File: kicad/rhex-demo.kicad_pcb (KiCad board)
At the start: 2 copper layers, 58 parts, among them J1 MCU power, M1 Motor_Servo, M2 Motor_Servo, M3 Motor_Servo, M4 Motor_Servo, M5 Motor_Servo, M6 Motor_Servo

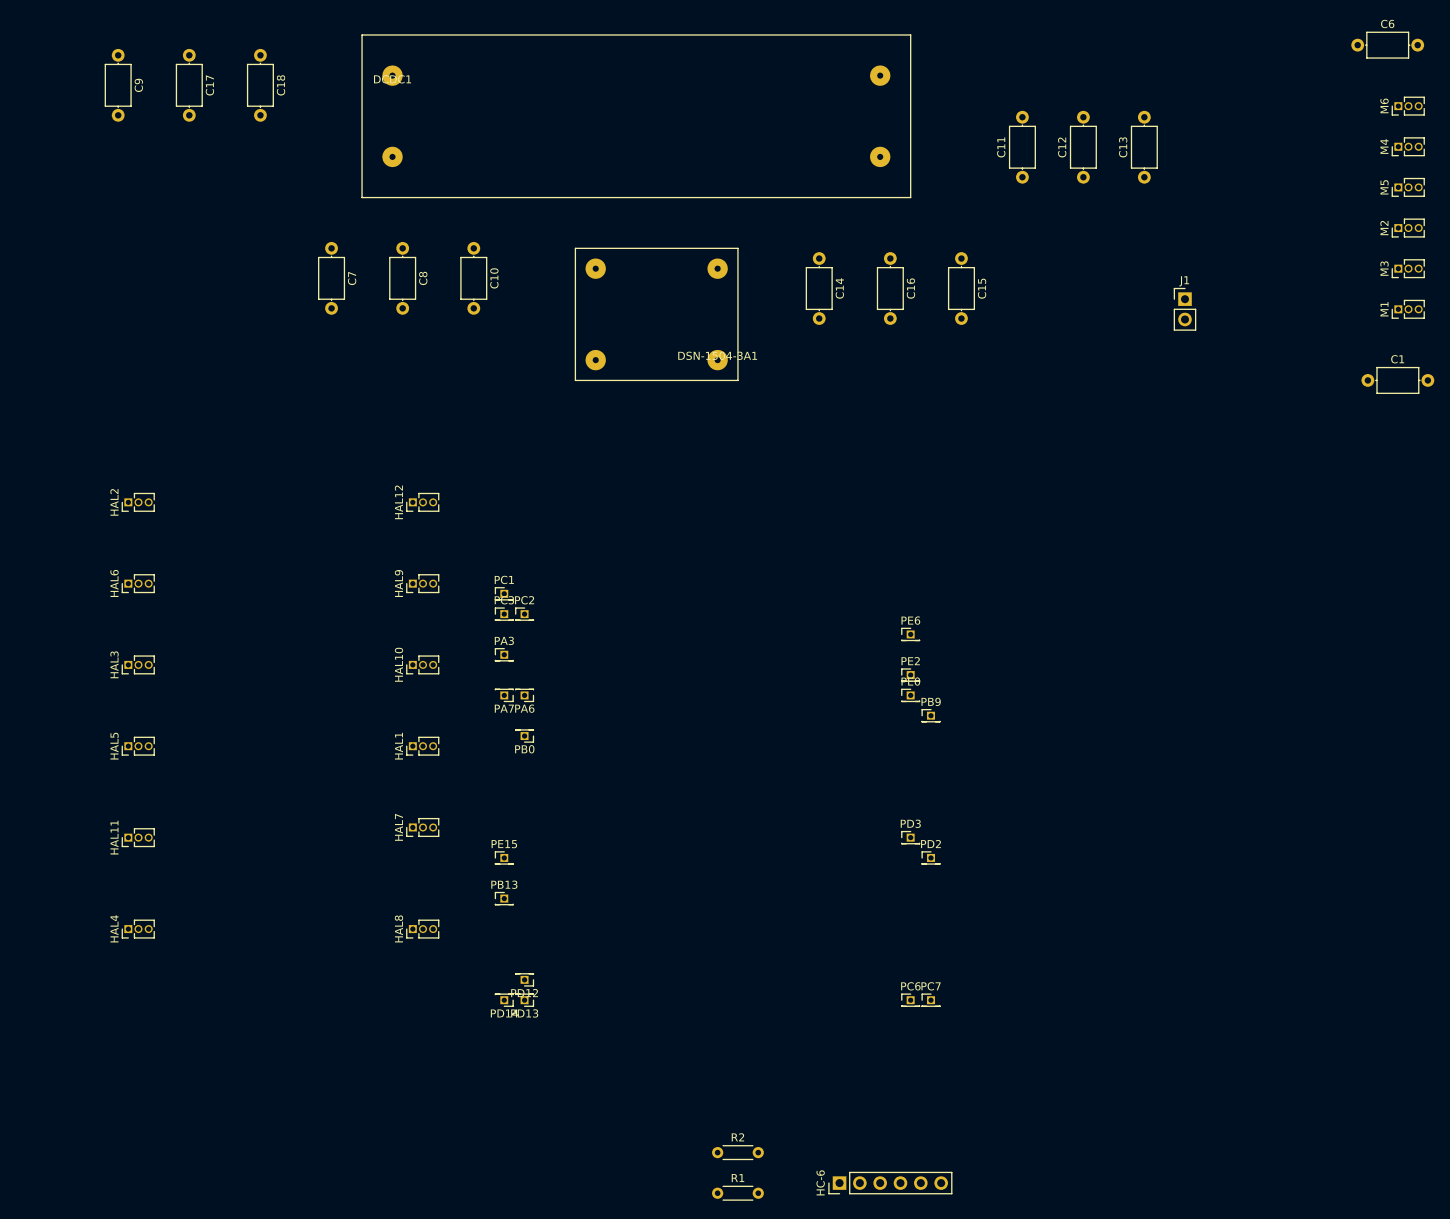
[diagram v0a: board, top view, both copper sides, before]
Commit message: pcb layout done, generated gerb files, generated report files
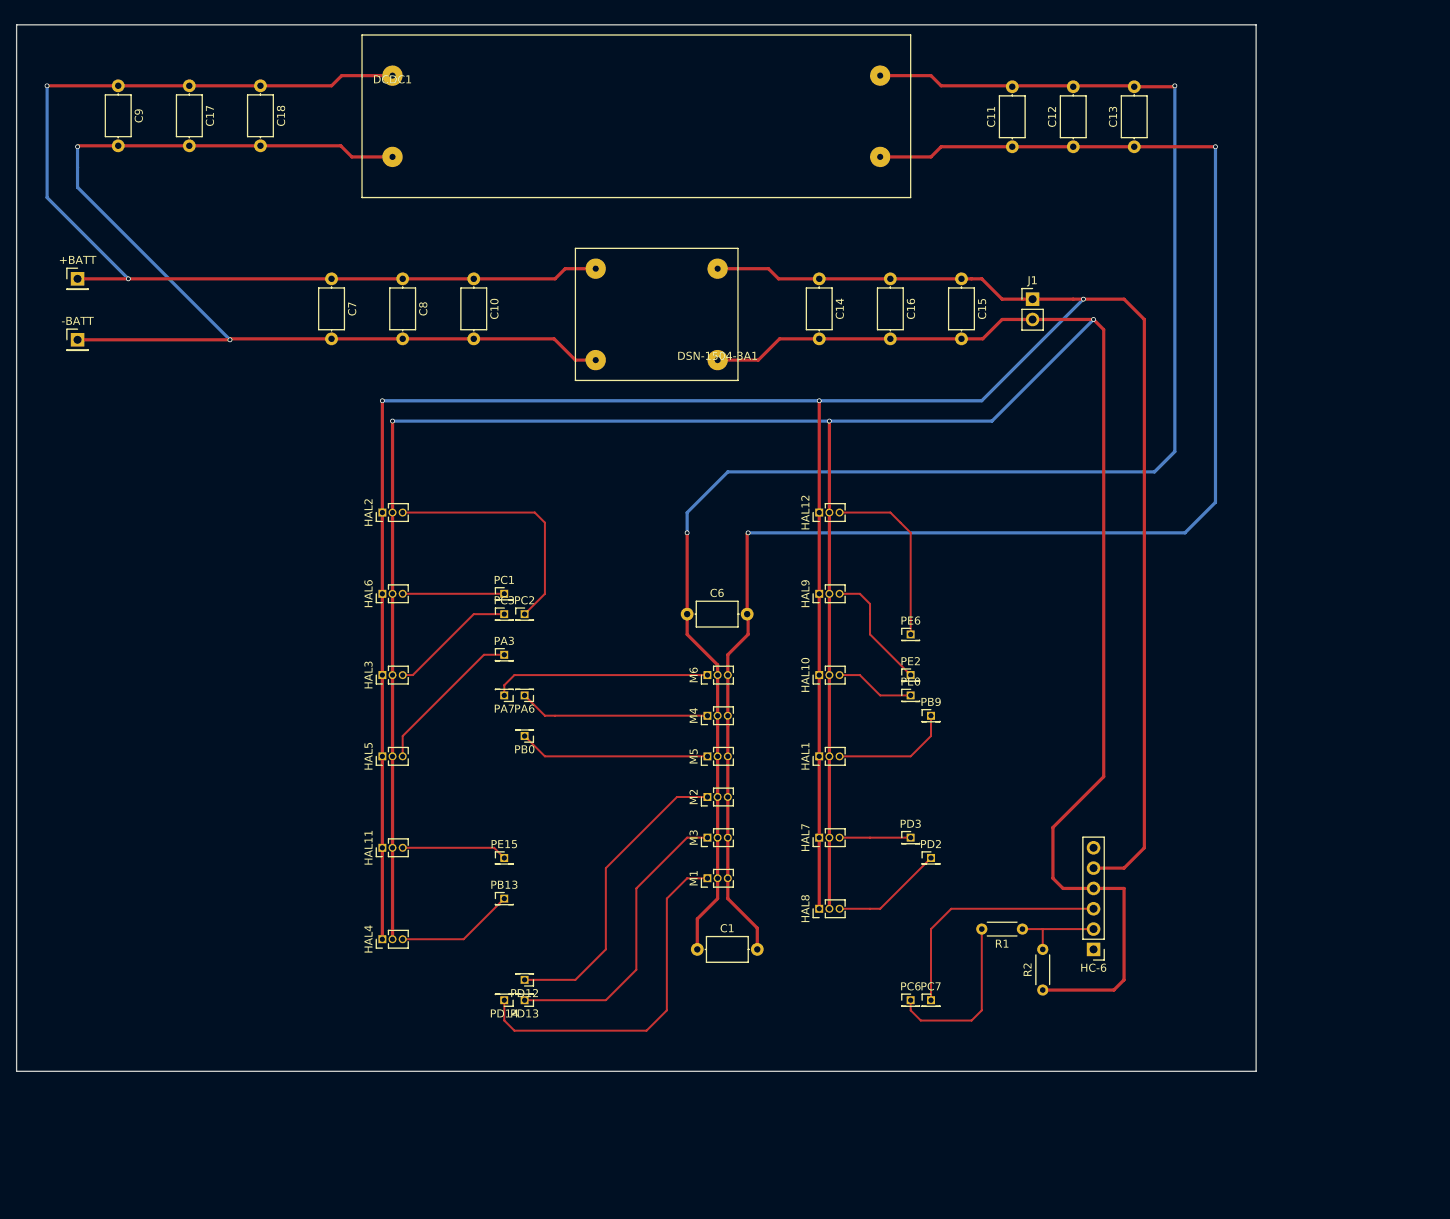
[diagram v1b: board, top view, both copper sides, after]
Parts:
- added +BATT: Pin_Header_Straight_1x01_Pitch2.54mm, Pin_Headers:Pin_Header_Straight_1x01_Pitch2.54mm, F.Cu at (55.9, 53.3)
- added -BATT: Pin_Header_Straight_1x01_Pitch2.54mm, Pin_Headers:Pin_Header_Straight_1x01_Pitch2.54mm, F.Cu at (55.9, 61.0)
- moved M1 111.9 mm to (134.6, 128.3)
- moved M2 111.9 mm to (134.6, 118.1)
- moved M3 111.9 mm to (134.6, 123.2)
- moved M4 111.9 mm to (134.6, 108.0)
- moved M5 111.9 mm to (134.6, 113.0)
- moved M6 111.9 mm to (134.6, 102.9)
- moved C6 109.9 mm to (132.1, 95.2)
- moved C1 109.9 mm to (133.3, 137.2)
- moved HAL8 50.9 mm to (148.6, 132.1)
- moved HAL1 50.8 mm to (148.6, 113.0)
- moved HAL10 50.8 mm to (148.6, 102.9)
- moved HAL12 50.8 mm to (148.6, 82.5)
- moved HAL7 50.8 mm to (148.6, 123.2)
- moved HAL9 50.8 mm to (148.6, 92.7)
- moved R1 50.4 mm to (174.0, 134.6), turned to 180 degrees
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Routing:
- net GND: track 0.00 -> 465.0 mm, vias 0 -> 4
- net Net-(C14-Pad1): track 0.00 -> 351.8 mm, vias 0 -> 3
- net Net-(C1-Pad1): track 0.00 -> 314.1 mm, vias 0 -> 3
- net +BATT: track 0.00 -> 137.3 mm, vias 0 -> 2
- net -BATT: track 0.00 -> 137.2 mm, vias 0 -> 2
- net Net-(M1-Pad1): track 0.00 -> 44.5 mm
- net Net-(M2-Pad1): track 0.00 -> 38.3 mm
- net Net-(M3-Pad1): track 0.00 -> 37.2 mm
- net Net-(HAL2-Pad3): track 0.00 -> 30.8 mm
- net (no net): track 0.00 -> 30.3 mm
- net Net-(M6-Pad1): track 0.00 -> 27.2 mm
- net Net-(M5-Pad1): track 0.00 -> 23.9 mm
- net Net-(M4-Pad1): track 0.00 -> 23.9 mm
- net Net-(HAL12-Pad3): track 0.00 -> 22.6 mm
- net Net-(PC6-Pad~): track 0.00 -> 21.4 mm
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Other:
- board outline added: 154.9 x 130.8 mm
- net class power added: clearance 0.2, trace_width 0.4, via_dia 0.6, via_drill 0.4

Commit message: minor changes to layout design, regenerated prints, changed sclk to 100MHz
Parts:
- moved C11 7.62 mm to (172.7, 29.2), turned to 270 degrees
- moved C12 7.62 mm to (180.3, 29.2), turned to 270 degrees
- moved C13 7.62 mm to (188.0, 29.2), turned to 270 degrees
- moved PD12 2.54 mm to (111.8, 138.4)
- moved PD13 2.54 mm to (111.8, 141.0)
- moved PD14 2.54 mm to (109.2, 141.0)
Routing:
- net GND: track 465.0 -> 613.2 mm, vias 4 -> 6
- net Net-(C1-Pad1): track 314.1 -> 206.3 mm, vias 3 -> 2
- net Net-(M1-Pad1): track 44.5 -> 39.8 mm
- net Net-(M3-Pad1): track 37.2 -> 36.2 mm

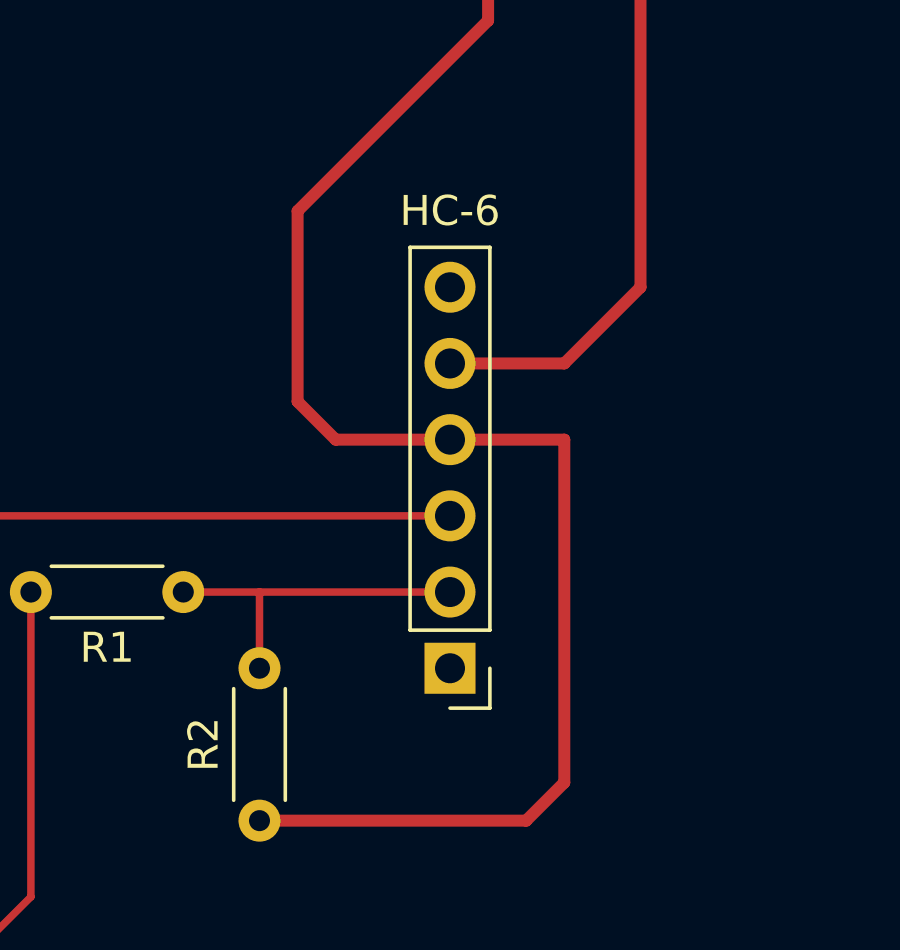
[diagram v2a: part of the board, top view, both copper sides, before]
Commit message: add leg detection functions
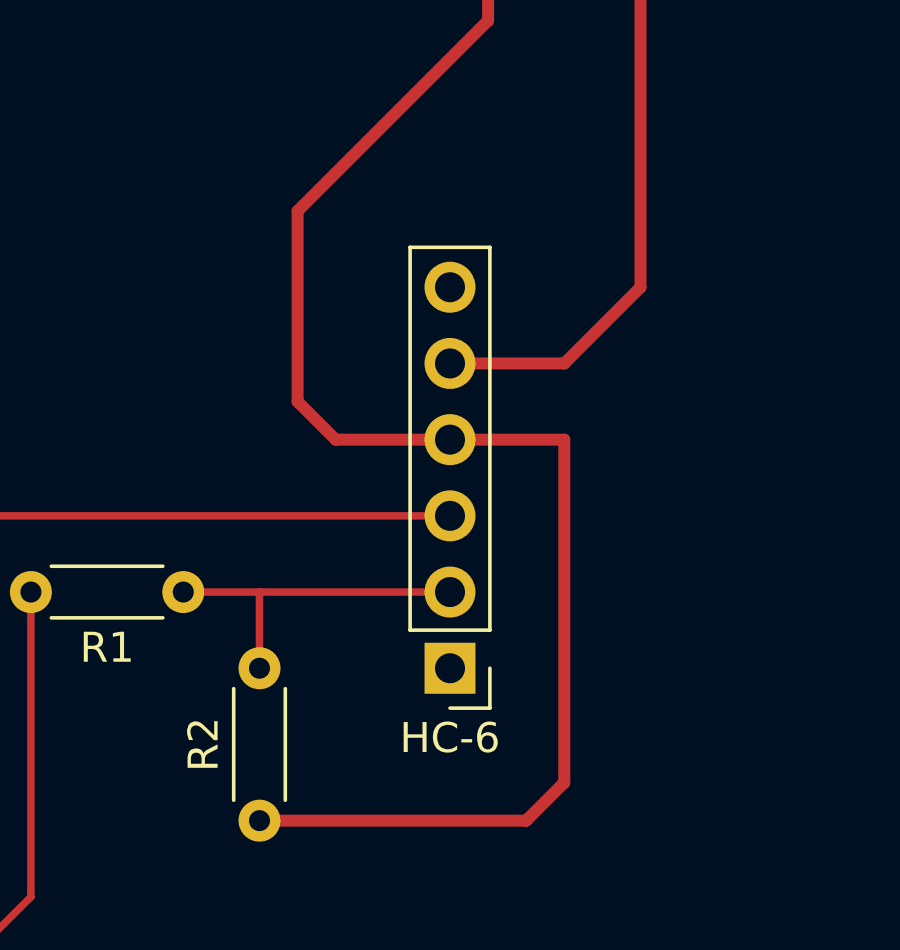
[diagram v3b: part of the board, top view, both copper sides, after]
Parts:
- HC-6: footprint Pin_Headers:Pin_Header_Straight_1x06_Pitch2.54mm -> Socket_Strips:Socket_Strip_Straight_1x06_Pitch2.54mm
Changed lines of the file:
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@@
     (links 68)
     (no_connects 43)
-    (area 40.679999 21.514999 203.275001 152.475001)
+    (area 48.184999 21.514999 203.275001 152.475001)
     (thickness 1.6)
     (drawings 6)
@@
       (net 2 GND))
   )
-  (module Pin_Headers:Pin_Header_Straight_1x06_Pitch2.54mm (layer F.Cu)
-    (at 182.88 137.16 180)
-    (descr "Through hole straight pin header, 1x06, 2.54mm pitch, single row")
-    (tags "Through hole pin header THT 1x06 2.54mm single row")
-    (fp_text reference HC-6 (at 0 15.24 180) (layer F.SilkS)
-      (effects (font (size 1 1) (thickness 0.15)))
-    )
-    (fp_text value HC-06-bluetooth (at 0 15.03 180) (layer F.Fab)
-      (effects (font (size 1 1) (thickness 0.15)))
-    )
-    (fp_line (start -0.635 -1.27) (end 1.27 -1.27) (layer F.Fab) (width 0.1))
-    (fp_line (start 1.27 -1.27) (end 1.27 13.97) (layer F.Fab) (width 0.1))
-    (fp_line (start 1.27 13.97) (end -1.27 13.97) (layer F.Fab) (width 0.1))
-    (fp_line (start -1.27 13.97) (end -1.27 -0.635) (layer F.Fab) (width 0.1))
-    (fp_line (start -1.27 -0.635) (end -0.635 -1.27) (layer F.Fab) (width 0.1))
-    (fp_line (start -1.33 14.03) (end 1.33 14.03) (layer F.SilkS) (width 0.12))
-    (fp_line (start -1.33 1.27) (end -1.33 14.03) (layer F.SilkS) (width 0.12))
-    (fp_line (start 1.33 1.27) (end 1.33 14.03) (layer F.SilkS) (width 0.12))
-    (fp_line (start -1.33 1.27) (end 1.33 1.27) (layer F.SilkS) (width 0.12))
-    (fp_line (start -1.33 0) (end -1.33 -1.33) (layer F.SilkS) (width 0.12))
-    (fp_line (start -1.33 -1.33) (end 0 -1.33) (layer F.SilkS) (width 0.12))
-    (fp_line (start -1.8 -1.8) (end -1.8 14.5) (layer F.CrtYd) (width 0.05))
-    (fp_line (start -1.8 14.5) (end 1.8 14.5) (layer F.CrtYd) (width 0.05))
-    (fp_line (start 1.8 14.5) (end 1.8 -1.8) (layer F.CrtYd) (width 0.05))
-    (fp_line (start 1.8 -1.8) (end -1.8 -1.8) (layer F.CrtYd) (width 0.05))
-    (fp_text user %R (at 0 6.35 270) (layer F.Fab)
-      (effects (font (size 1 1) (thickness 0.15)))
-    )
-    (pad 1 thru_hole rect (at 0 0 180) (size 1.7 1.7) (drill 1) (layers *.Cu *.Mask))
-    (pad 2 thru_hole oval (at 0 2.54 180) (size 1.7 1.7) (drill 1) (layers *.Cu *.Mask))
-    (pad 3 thru_hole oval (at 0 5.08 180) (size 1.7 1.7) (drill 1) (layers *.Cu *.Mask))
-    (pad 4 thru_hole oval (at 0 7.62 180) (size 1.7 1.7) (drill 1) (layers *.Cu *.Mask))
-    (pad 5 thru_hole oval (at 0 10.16 180) (size 1.7 1.7) (drill 1) (layers *.Cu *.Mask))
-    (pad 6 thru_hole oval (at 0 12.7 180) (size 1.7 1.7) (drill 1) (layers *.Cu *.Mask))
-    (model ${KISYS3DMOD}/Pin_Headers.3dshapes/Pin_Header_Straight_1x06_Pitch2.54mm.wrl
-      (at (xyz 0 0 0))
-      (scale (xyz 1 1 1))
-      (rotate (xyz 0 0 0))
-    )
-  )
   (module Pin_Headers:Pin_Header_Straight_1x02_Pitch2.54mm (layer F.Cu)
     (at 175.26 55.88)
@@
     )
   )
+  (module Socket_Strips:Socket_Strip_Straight_1x06_Pitch2.54mm (layer F.Cu)
+    (at 182.88 137.16 180)
+    (descr "Through hole straight socket strip, 1x06, 2.54mm pitch, single row")
+    (tags "Through hole socket strip THT 1x06 2.54mm single row")
+    (fp_text reference HC-6 (at 0 -2.33 180) (layer F.SilkS)
+      (effects (font (size 1 1) (thickness 0.15)))
+    )
+    (fp_text value HC-06-bluetooth (at 0 15.03 180) (layer F.Fab)
+      (effects (font (size 1 1) (thickness 0.15)))
+    )
+    (fp_line (start -1.27 -1.27) (end -1.27 13.97) (layer F.Fab) (width 0.1))
+    (fp_line (start -1.27 13.97) (end 1.27 13.97) (layer F.Fab) (width 0.1))
+    (fp_line (start 1.27 13.97) (end 1.27 -1.27) (layer F.Fab) (width 0.1))
+    (fp_line (start 1.27 -1.27) (end -1.27 -1.27) (layer F.Fab) (width 0.1))
+    (fp_line (start -1.33 1.27) (end -1.33 14.03) (layer F.SilkS) (width 0.12))
+    (fp_line (start -1.33 14.03) (end 1.33 14.03) (layer F.SilkS) (width 0.12))
+    (fp_line (start 1.33 14.03) (end 1.33 1.27) (layer F.SilkS) (width 0.12))
+    (fp_line (start 1.33 1.27) (end -1.33 1.27) (layer F.SilkS) (width 0.12))
+    (fp_line (start -1.33 0) (end -1.33 -1.33) (layer F.SilkS) (width 0.12))
+    (fp_line (start -1.33 -1.33) (end 0 -1.33) (layer F.SilkS) (width 0.12))
+    (fp_line (start -1.8 -1.8) (end -1.8 14.5) (layer F.CrtYd) (width 0.05))
+    (fp_line (start -1.8 14.5) (end 1.8 14.5) (layer F.CrtYd) (width 0.05))
+    (fp_line (start 1.8 14.5) (end 1.8 -1.8) (layer F.CrtYd) (width 0.05))
+    (fp_line (start 1.8 -1.8) (end -1.8 -1.8) (layer F.CrtYd) (width 0.05))
+    (fp_text user %R (at 0 -2.33 180) (layer F.Fab)
+      (effects (font (size 1 1) (thickness 0.15)))
+    )
+    (pad 1 thru_hole rect (at 0 0 180) (size 1.7 1.7) (drill 1) (layers *.Cu *.Mask))
+    (pad 2 thru_hole oval (at 0 2.54 180) (size 1.7 1.7) (drill 1) (layers *.Cu *.Mask))
+    (pad 3 thru_hole oval (at 0 5.08 180) (size 1.7 1.7) (drill 1) (layers *.Cu *.Mask))
+    (pad 4 thru_hole oval (at 0 7.62 180) (size 1.7 1.7) (drill 1) (layers *.Cu *.Mask))
+    (pad 5 thru_hole oval (at 0 10.16 180) (size 1.7 1.7) (drill 1) (layers *.Cu *.Mask))
+    (pad 6 thru_hole oval (at 0 12.7 180) (size 1.7 1.7) (drill 1) (layers *.Cu *.Mask))
+    (model ${KISYS3DMOD}/Socket_Strips.3dshapes/Socket_Strip_Straight_1x06_Pitch2.54mm.wrl
+      (at (xyz 0 -0.25 0))
+      (scale (xyz 1 1 1))
+      (rotate (xyz 0 0 270))
+    )
+  )
